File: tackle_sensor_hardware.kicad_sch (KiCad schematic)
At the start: 82 parts, among them J1 Conn_01x02_Male, J2 Conn_01x04_Male, J3 Conn_01x03_Male, J4 Conn_ARM_JTAG_SWD_10, Q1 DMP4051LK3, Q2 2N7002K, Q3 2N7002K, Q4 2N7002K, Q5 2N7002K, Q6 2N7002K, Q7 2N7002K, Q9 CSD19538Q3A, SW1 PTS645SL43SMTR92 LFS, SW2 SW_DIP_x01, T1 DRQ125-330-R, U1 LIS2DE12, U2 STM32G031Fx, U3 LM3488, U4 LD1117S33TR_SOT223

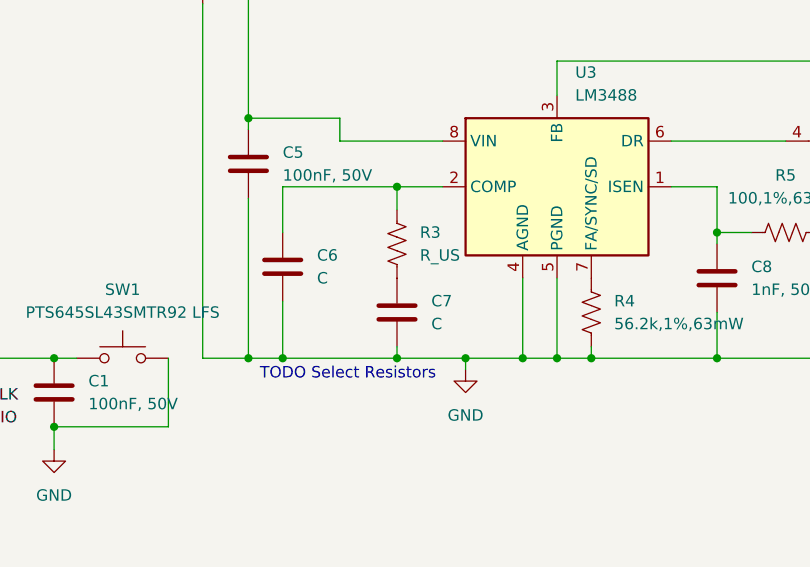
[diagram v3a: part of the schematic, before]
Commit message: finish route, add release pacakage
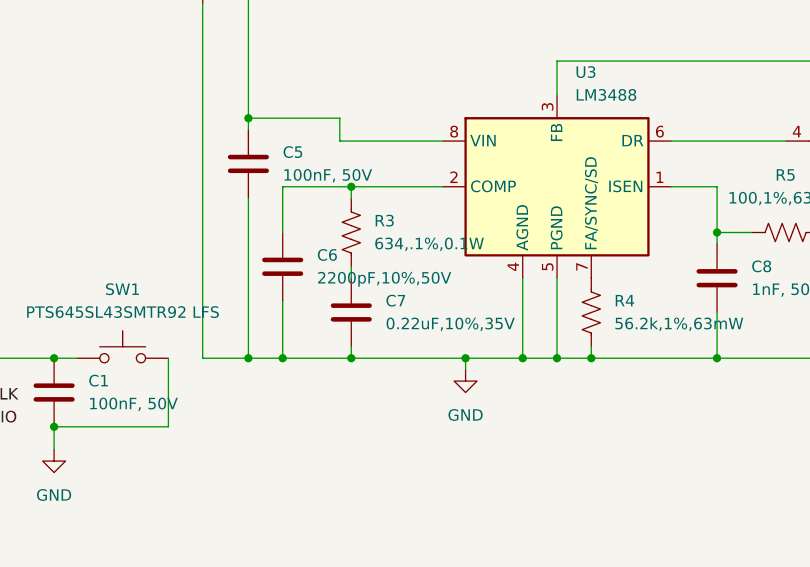
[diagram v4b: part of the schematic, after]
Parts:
- C6: value C -> 2200pF,10%,50V; MPN (none) -> 0402B222K500CT
- C7: value C -> 0.22uF,10%,35V; MPN (none) -> GRT155R6YA224KE01D
- R3: value R_US -> 634,.1%,0.1W; MPN (none) -> ERJ-2RKF6340X
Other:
- note removed: "TODO Select Resistors"
- moved on the sheet: C7, R3
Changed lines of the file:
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@@
   (junction (at 246.38 162.56) (diameter 0) (color 0 0 0 0)
   )
-  (junction (at 105.41 93.98) (diameter 0) (color 0 0 0 0)
+  (junction (at 100.33 93.98) (diameter 0) (color 0 0 0 0)
   )
   (junction (at 265.43 45.72) (diameter 0) (color 0 0 0 0)
   )
-  (junction (at 105.41 74.93) (diameter 0) (color 0 0 0 0)
+  (junction (at 100.33 74.93) (diameter 0) (color 0 0 0 0)
   )
   (junction (at 321.31 162.56) (diameter 0) (color 0 0 0 0)
@@
     (stroke (width 0) (type default) (color 0 0 0 0))
   )
-  (wire (pts (xy 105.41 92.71) (xy 105.41 93.98))
+  (wire (pts (xy 100.33 92.71) (xy 100.33 93.98))
     (stroke (width 0) (type default) (color 0 0 0 0))
   )
@@
     (stroke (width 0) (type default) (color 0 0 0 0))
   )
-  (wire (pts (xy 110.49 74.93) (xy 105.41 74.93))
+  (wire (pts (xy 110.49 74.93) (xy 100.33 74.93))
     (stroke (width 0) (type default) (color 0 0 0 0))
   )
@@
     (stroke (width 0) (type default) (color 0 0 0 0))
   )
+  (wire (pts (xy 100.33 83.82) (xy 100.33 85.09))
+    (stroke (width 0) (type default) (color 0 0 0 0))
+  )
   (wire (pts (xy 243.84 58.42) (xy 254 58.42))
     (stroke (width 0) (type default) (color 0 0 0 0))
@@
     (stroke (width 0) (type default) (color 0 0 0 0))
   )
-  (wire (pts (xy 105.41 74.93) (xy 105.41 77.47))
+  (wire (pts (xy 100.33 74.93) (xy 100.33 76.2))
     (stroke (width 0) (type default) (color 0 0 0 0))
   )
@@
     (stroke (width 0) (type default) (color 0 0 0 0))
   )
-  (wire (pts (xy 105.41 93.98) (xy 113.03 93.98))
+  (wire (pts (xy 100.33 93.98) (xy 113.03 93.98))
     (stroke (width 0) (type default) (color 0 0 0 0))
   )
@@
     (stroke (width 0) (type default) (color 0 0 0 0))
   )
-  (wire (pts (xy 92.71 93.98) (xy 105.41 93.98))
+  (wire (pts (xy 92.71 93.98) (xy 100.33 93.98))
     (stroke (width 0) (type default) (color 0 0 0 0))
   )
@@
     (stroke (width 0) (type default) (color 0 0 0 0))
   )
-  (wire (pts (xy 105.41 74.93) (xy 92.71 74.93))
+  (wire (pts (xy 100.33 74.93) (xy 92.71 74.93))
     (stroke (width 0) (type default) (color 0 0 0 0))
   )
@@
   (text "+12V LED Output\nCurrent - Trip: 1.75 A\nCurrent - Hold: 350 mA\nTime to Trip: 100 ms"
     (at 293.37 118.11 0)
-    (effects (font (size 1.27 1.27)) (justify left bottom))
-  )
-  (text "TODO Select Resistors" (at 90.17 96.52 0)
     (effects (font (size 1.27 1.27)) (justify left bottom))
   )
@@
     )
   )
-  (symbol (lib_id "Device:C") (at 105.41 88.9 0) (unit 1)
-    (in_bom yes) (on_board yes) (fields_autoplaced)
-    (property "Reference" "C7" (id 0) (at 109.22 87.6299 0)
-      (effects (font (size 1.27 1.27)) (justify left))
-    )
-    (property "Value" "C" (id 1) (at 109.22 90.1699 0)
-      (effects (font (size 1.27 1.27)) (justify left))
-    )
-    (property "Footprint" "Capacitor_SMD:C_0402_1005Metric" (id 2) (at 106.3752 92.71 0)
-      (effects (font (size 1.27 1.27)) hide)
-    )
-    (property "Datasheet" "~" (id 3) (at 105.41 88.9 0)
+  (symbol (lib_id "Device:C") (at 100.33 88.9 0) (unit 1)
+    (in_bom yes) (on_board yes) (fields_autoplaced)
+    (property "Reference" "C7" (id 0) (at 104.14 87.6299 0)
+      (effects (font (size 1.27 1.27)) (justify left))
+    )
+    (property "Value" "0.22uF,10%,35V" (id 1) (at 104.14 90.1699 0)
+      (effects (font (size 1.27 1.27)) (justify left))
+    )
+    (property "Footprint" "Capacitor_SMD:C_0402_1005Metric" (id 2) (at 101.2952 92.71 0)
+      (effects (font (size 1.27 1.27)) hide)
+    )
+    (property "Datasheet" "https://search.murata.co.jp/Ceramy/image/img/A01X/partnumbering_e_02.pdf" (id 3) (at 100.33 88.9 0)
+      (effects (font (size 1.27 1.27)) hide)
+    )
+    (property "MPN" "GRT155R6YA224KE01D" (id 4) (at 100.33 88.9 0)
       (effects (font (size 1.27 1.27)) hide)
     )
@@
     (pin "2")
   )
-  (symbol (lib_id "Device:R_US") (at 105.41 81.28 0) (unit 1)
-    (in_bom yes) (on_board yes) (fields_autoplaced)
-    (property "Reference" "R3" (id 0) (at 107.95 80.0099 0)
-      (effects (font (size 1.27 1.27)) (justify left))
-    )
-    (property "Value" "R_US" (id 1) (at 107.95 82.5499 0)
-      (effects (font (size 1.27 1.27)) (justify left))
-    )
-    (property "Footprint" "Resistor_SMD:R_0402_1005Metric" (id 2) (at 106.426 81.534 90)
-      (effects (font (size 1.27 1.27)) hide)
-    )
-    (property "Datasheet" "~" (id 3) (at 105.41 81.28 0)
+  (symbol (lib_id "Device:R_US") (at 100.33 80.01 0) (unit 1)
+    (in_bom yes) (on_board yes) (fields_autoplaced)
+    (property "Reference" "R3" (id 0) (at 102.87 78.7399 0)
+      (effects (font (size 1.27 1.27)) (justify left))
+    )
+    (property "Value" "634,.1%,0.1W" (id 1) (at 102.87 81.2799 0)
+      (effects (font (size 1.27 1.27)) (justify left))
+    )
+    (property "Footprint" "Resistor_SMD:R_0402_1005Metric" (id 2) (at 101.346 80.264 90)
+      (effects (font (size 1.27 1.27)) hide)
+    )
+    (property "Datasheet" "https://industrial.panasonic.com/cdbs/www-data/pdf/RDA0000/AOA0000C304.pdf" (id 3) (at 100.33 80.01 0)
+      (effects (font (size 1.27 1.27)) hide)
+    )
+    (property "MPN" "ERJ-2RKF6340X" (id 4) (at 100.33 80.01 0)
       (effects (font (size 1.27 1.27)) hide)
     )
@@
       (effects (font (size 1.27 1.27)) (justify left))
     )
-    (property "Value" "C" (id 1) (at 96.52 85.0899 0)
+    (property "Value" "2200pF,10%,50V" (id 1) (at 96.52 85.0899 0)
       (effects (font (size 1.27 1.27)) (justify left))
     )
@@
       (effects (font (size 1.27 1.27)) hide)
     )
-    (property "Datasheet" "~" (id 3) (at 92.71 83.82 0)
+    (property "Datasheet" "https://www.passivecomponent.com/wp-content/uploads/datasheet/WTC_MLCC_General_Purpose.pdf" (id 3) (at 92.71 83.82 0)
+      (effects (font (size 1.27 1.27)) hide)
+    )
+    (property "MPN" "0402B222K500CT" (id 4) (at 92.71 83.82 0)
       (effects (font (size 1.27 1.27)) hide)
     )
@@
     )
     (path "/84b2e8c0-f17e-4c6f-9a69-984374f700ab"
-      (reference "C6") (unit 1) (value "C") (footprint "Capacitor_SMD:C_0402_1005Metric")
+      (reference "C6") (unit 1) (value "2200pF,10%,50V") (footprint "Capacitor_SMD:C_0402_1005Metric")
     )
     (path "/43efc653-c82a-45e7-8b5f-a91e903fb8c8"
-      (reference "C7") (unit 1) (value "C") (footprint "Capacitor_SMD:C_0402_1005Metric")
+      (reference "C7") (unit 1) (value "0.22uF,10%,35V") (footprint "Capacitor_SMD:C_0402_1005Metric")
     )
     (path "/109a1cc3-2724-4e09-bfdd-2cd7cc22195e"
@@
     )
     (path "/776bfe19-e581-4d73-80c0-1958bddf5275"
-      (reference "R3") (unit 1) (value "R_US") (footprint "Resistor_SMD:R_0402_1005Metric")
+      (reference "R3") (unit 1) (value "634,.1%,0.1W") (footprint "Resistor_SMD:R_0402_1005Metric")
     )
     (path "/2dec3f16-d443-4e35-ae47-c02c1ae03a32"

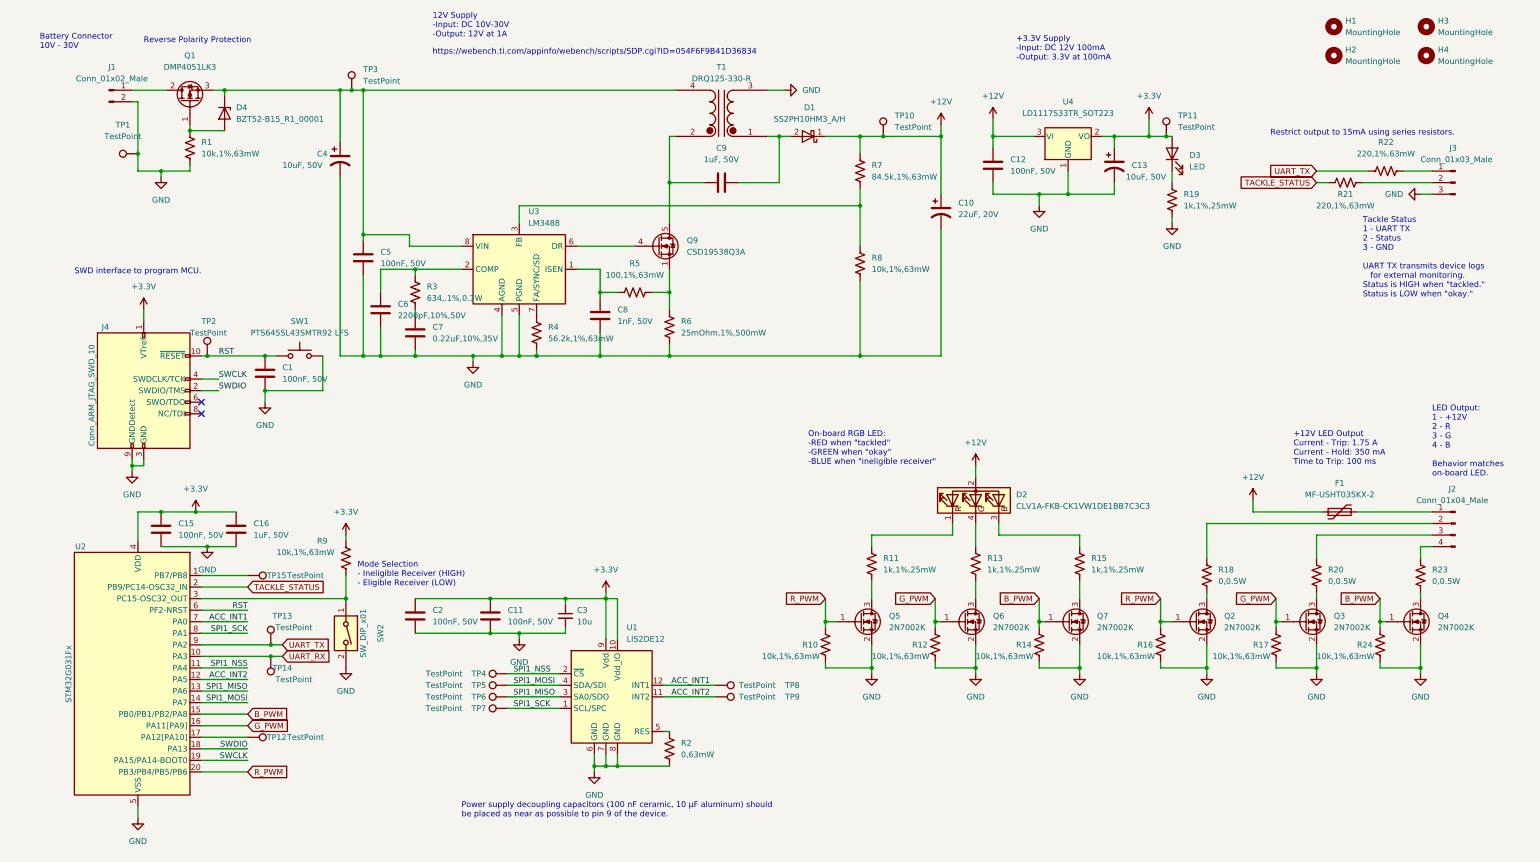
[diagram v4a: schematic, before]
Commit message: updated some parts with instock components
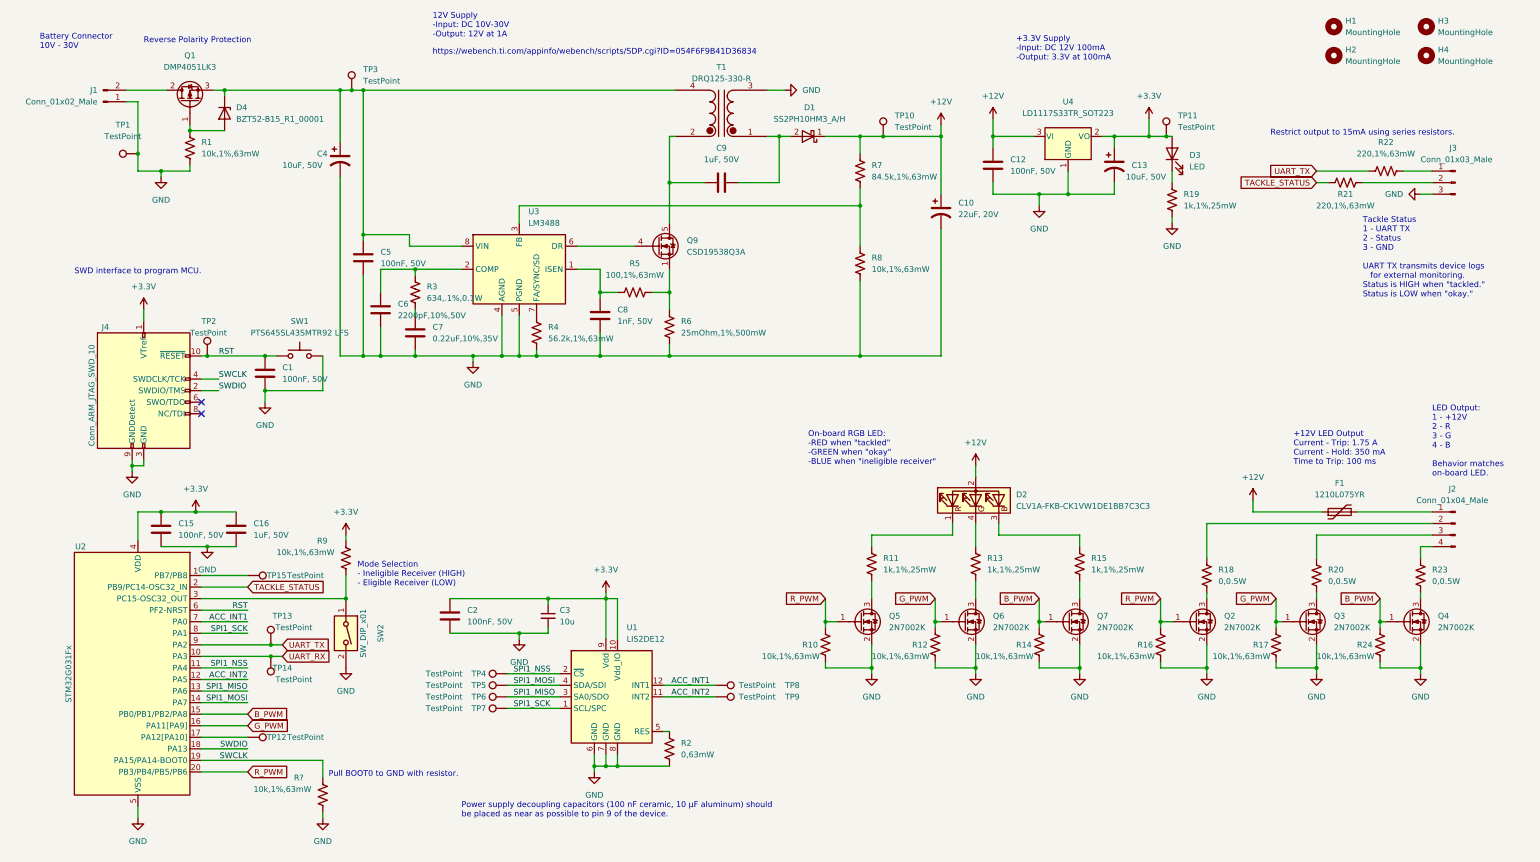
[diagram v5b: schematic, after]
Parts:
- removed C11: 100nF, 50V, Capacitor_SMD:C_0805_2012Metric, symbol Device:C
- added R?: 10k,1%,63mW, Resistor_SMD:R_0402_1005Metric, symbol Device:R_US
- C1: Field5 (none) -> C49678
- C10: JLCPN (none) -> C215761
- C12, C15, C2, C5: JLCPN (none) -> C49678
- C13, C4: JLCPN (none) -> C308830
- C16, C9: JLCPN (none) -> C90540; MPN C1608X5R1H105K080AB -> 0603B105K500NT
- C6: JLCPB (none) -> C338130
- C7: JLCPN (none) -> C694490; MPN GRT155R6YA224KE01D -> CGA2B1X7R1V224KT000F
- C8: JLCPN (none) -> C1523; MPN GRM1555C1H102JA01J -> 0402B102K500NT
- D3: JLCPN (none) -> C72038; MPN (none) -> 19-213/Y2C-CQ2R2L/3T(CY)
- F1: value MF-USHT035KX-2 -> 1210L075YR; JLCPN (none) -> C207046; MPN MF-USHT035KX-2 -> 1210L075YR
- Q1: JLCPN (none) -> C397952; MPN (none) -> DMP4051LK3-13
- U1: JLCPN (none) -> C155639; MPN (none) -> LIS2DE12TR
- U3: JLCPN (none) -> C80773; MPN (none) -> LM3488MM/NOPB
- U4: JLCPN (none) -> C86781; MPN (none) -> LD1117S33TR
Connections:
- net GND: now also J1.1 (Pin_1), R?.2; no longer J1.2 (Pin_2)
- net SWCLK: now also R?.1
- net at Q1.2 (D): now also J1.2 (Pin_2); no longer J1.1 (Pin_1)
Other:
- note added: "Pull BOOT0 to GND with resistor."
- moved on the sheet: C2, C3, J1

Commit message: Updating schematic and layout for manufacture with LCSC.
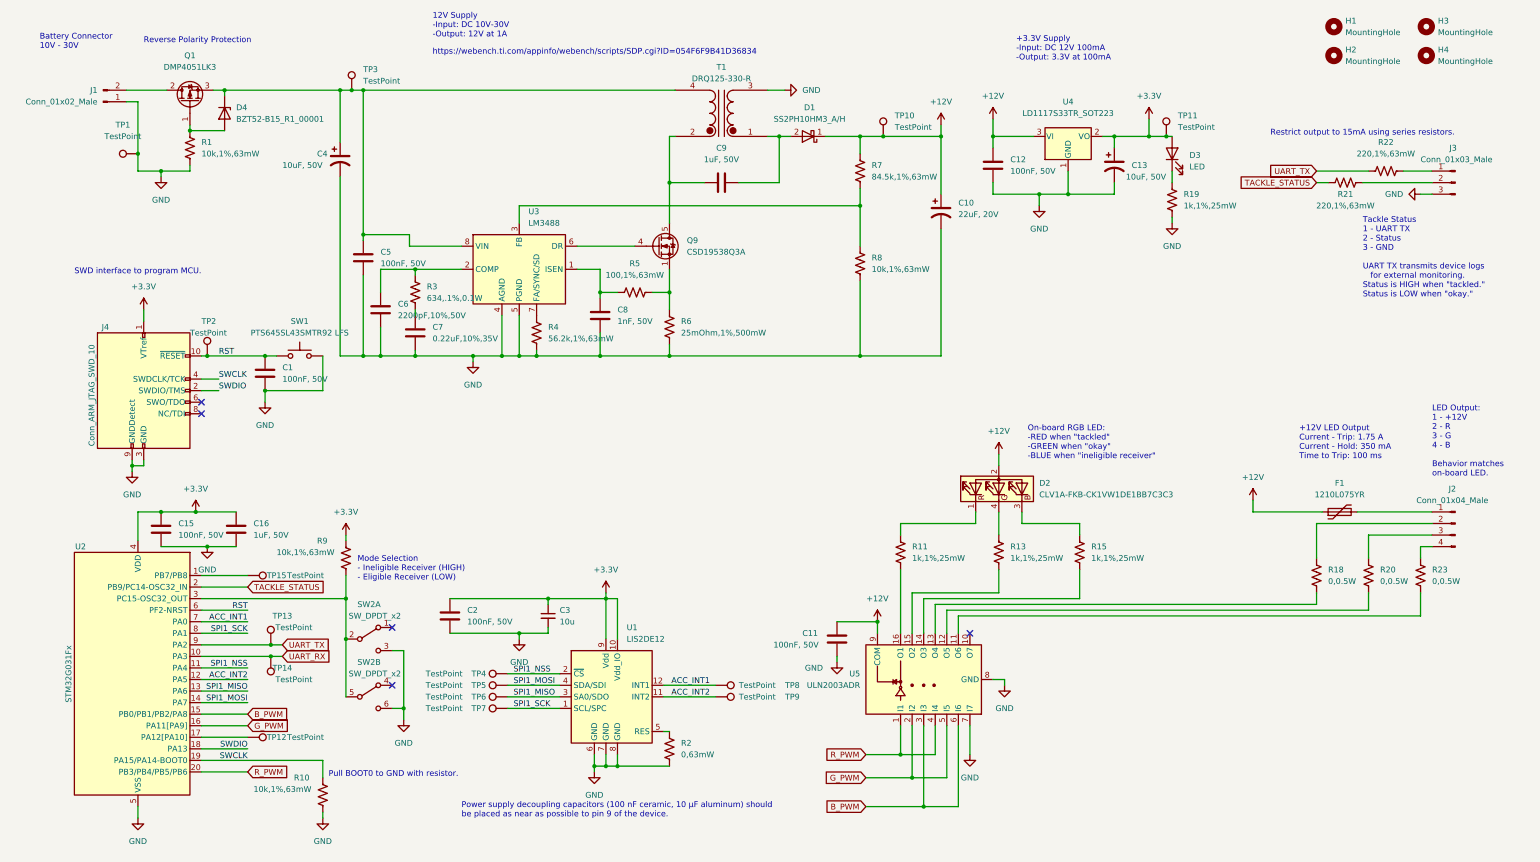
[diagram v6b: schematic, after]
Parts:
- removed Q2, Q3, Q4, Q5, Q6, Q7: 2N7002K, Package_TO_SOT_SMD:SOT-23, symbol Transistor_FET:2N7002K
- removed R10, R12, R14, R16, R17, R24: 10k,1%,63mW, Resistor_SMD:R_0402_1005Metric, symbol Device:R_US
- removed SW2: SW_DIP_x01, Button_Switch_SMD:SW_DIP_SPSTx01_Slide_6.7x4.1mm_W8.61mm_P2.54mm_LowProfile, symbol Switch:SW_DIP_x01
- added C11: 100nF, 50V, Capacitor_SMD:C_0805_2012Metric, symbol Device:C
- added SW2: SW_DPDT_x2, symbol Switch:SW_DPDT_x2
- added U5: ULN2003ADR, Package_SO:SOIC-16_3.9x9.9mm_P1.27mm, symbol Transistor_Array:ULN2003A
- J1: JLCPN (none) -> C158012; MPN (none) -> B2B-XH-A(LF)(SN)
- J2: JLCPN (none) -> C144395; MPN (none) -> B4B-XH-A(LF)(SN)
- J3: JLCPN (none) -> C144394; MPN (none) -> B3B-XH-A(LF)(SN)
- J4: footprint Connector_PinHeader_1.27mm:PinHeader_2x05_P1.27mm_Vertical -> rfc_footprint_lib:20021121-00010C4LF; JLCPN (none) -> C150517; MPN (none) -> 20021121-00010C4LF
- TP12, TP13, TP14, TP15, TP4, TP5, TP6, TP7, TP8, TP9: footprint TestPoint:TestPoint_Pad_D1.5mm -> TestPoint:TestPoint_Pad_D1.0mm
- gave numbers to parts that had none: 1
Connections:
- net +12V: now also C11.1, U5.9 (COM)
- net B_PWM: now also U5.3 (I3), U5.6 (I6)
- net GND: now also C11.2, SW2.3 (C), SW2.6 (C), U5.7 (I7), U5.8 (GND)
- net G_PWM: now also U5.2 (I2), U5.5 (I5)
- net R_PWM: now also U5.1 (I1), U5.4 (I4)
- net at R13.2: now also U5.15 (O2)
- net at R18.1: now also U5.13 (O4)
- net at R15.2: now also U5.14 (O3)
- net at R9.2, U2.3 (PC15-OSC32_OUT): now also SW2.2 (B), SW2.5 (B)
- net at R23.1: now also U5.11 (O6)
- net at R11.2: now also U5.16 (O1)
- net at R20.1: now also U5.12 (O5)
- no-connect marks 2 -> 5
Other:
- moved on the sheet: D2, R11, R13, R15, R18, R20
